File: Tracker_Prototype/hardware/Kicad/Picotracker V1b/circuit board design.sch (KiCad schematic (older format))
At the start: 57 parts, among them IC7 SPV1040, J1 Conn_01x06, J2 GND, J3 +SOL, J4 BATT_V+, J5 BATT_GND, Q1 Q_PMOS_DGS, Q2 Q_PMOS_DGS, SW1 SW_Push, U2 TPS62740, U3 CMWX1ZZABZ-078, U4 MAX-M8C, U6 MS5607-02BA

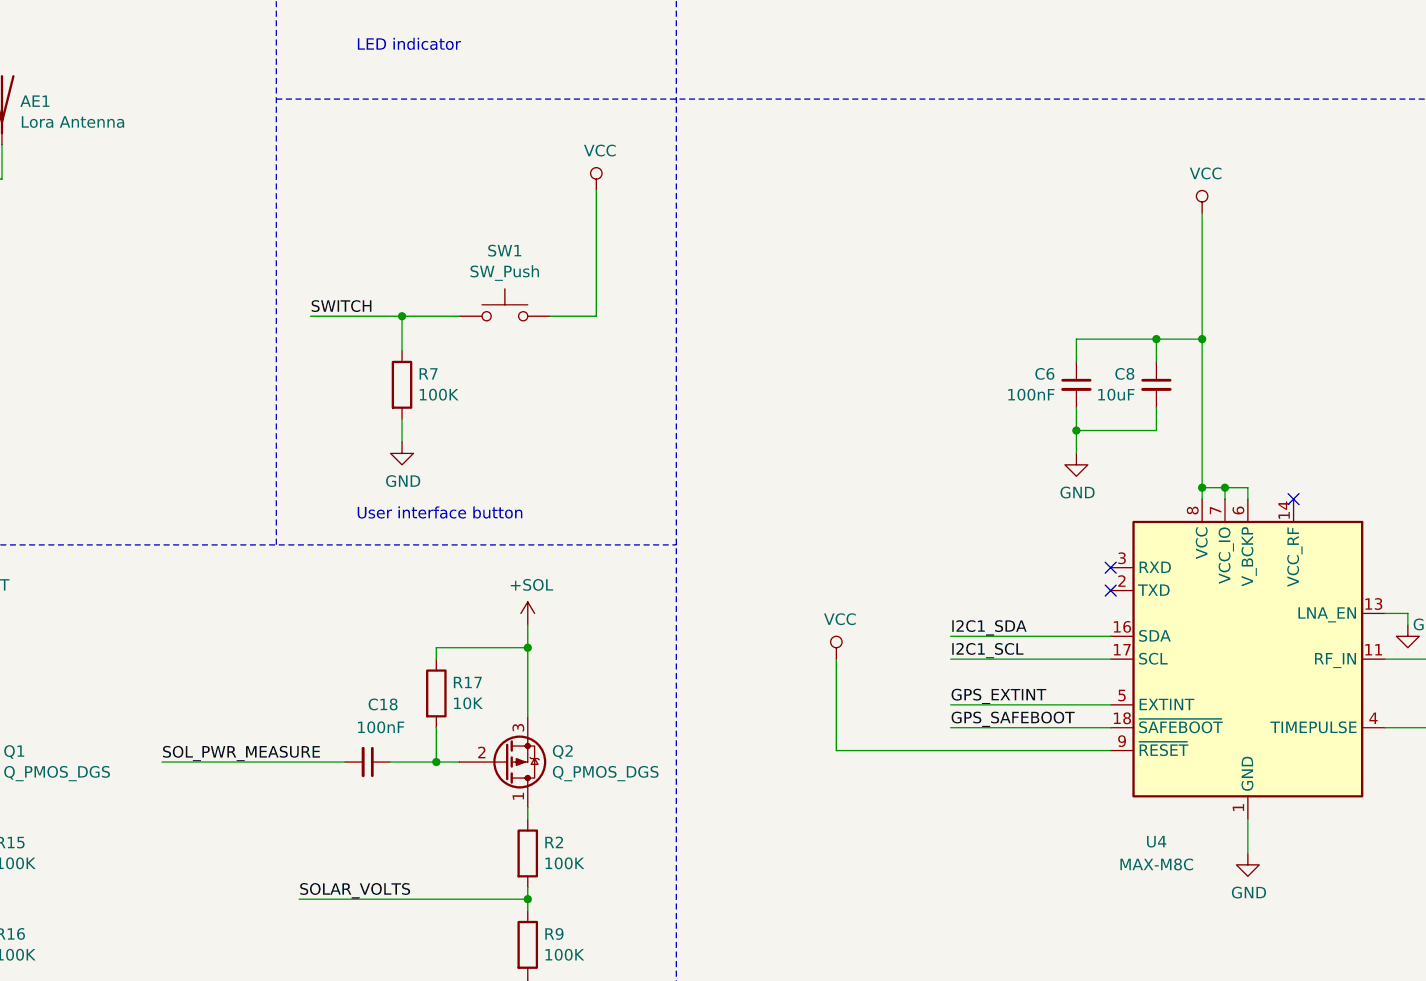
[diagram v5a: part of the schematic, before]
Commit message: Power GPS through SENSE_VCC
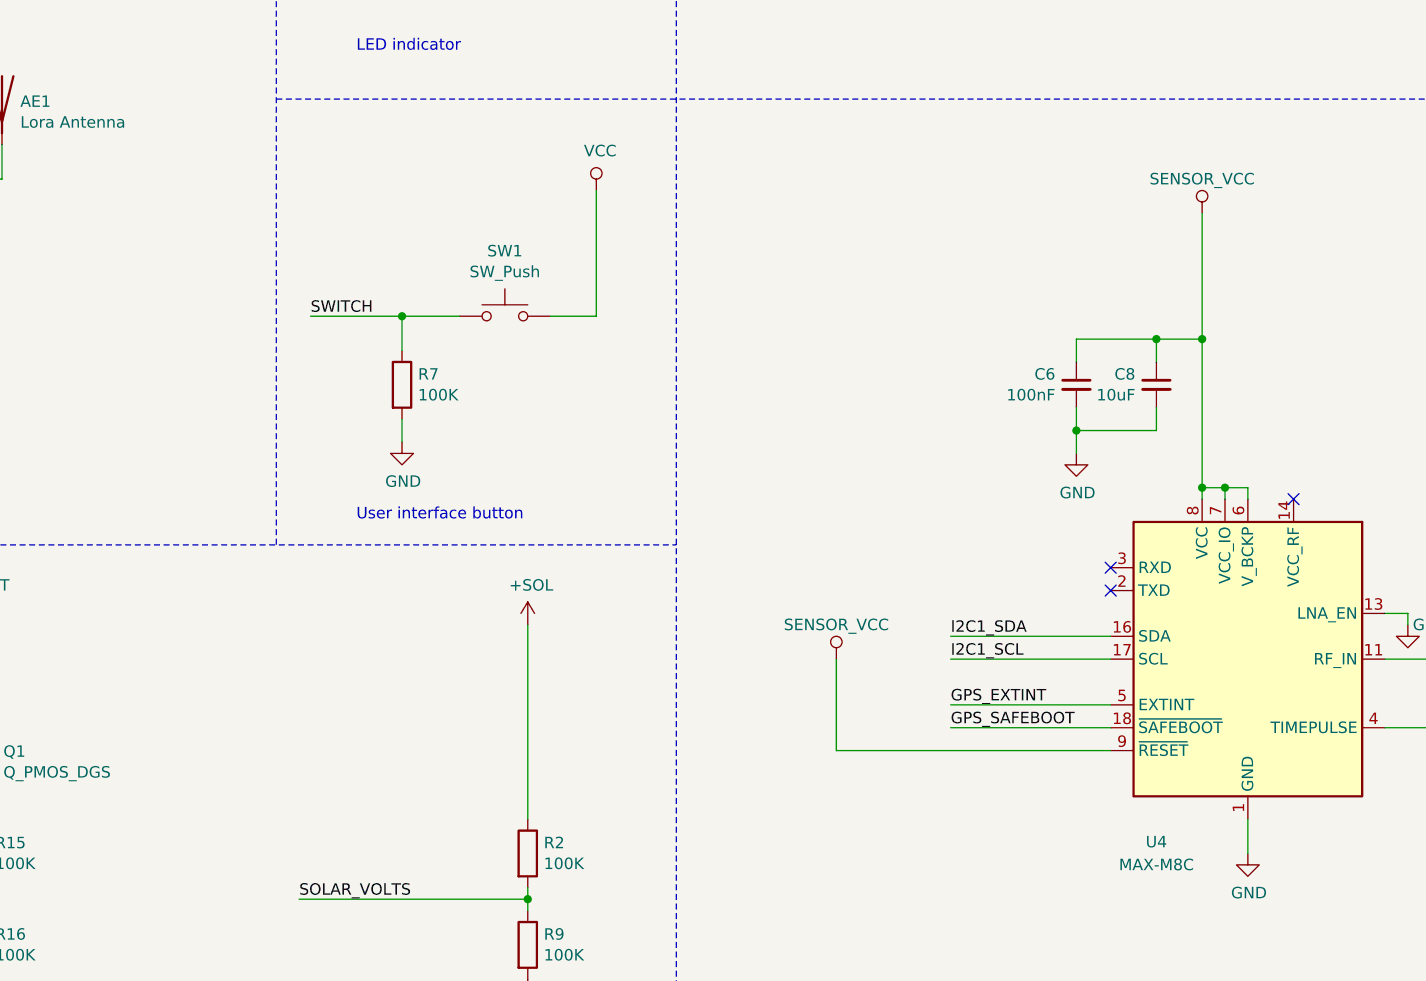
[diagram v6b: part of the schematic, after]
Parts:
- removed C18: 100nF, Capacitor_SMD:C_0402_1005Metric, symbol Device:C_Small
- removed Q2: Q_PMOS_DGS, Package_TO_SOT_SMD:SOT-23, symbol Device:Q_PMOS_DGS
- removed R17: 10K, Resistor_SMD:R_0402_1005Metric, symbol Device:R
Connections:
- net +SOL: now also R2.1
- net SENSOR_VCC: now also C6.1, C8.1, U4.6 (V_BCKP), U4.7 (VCC_IO), U4.8 (VCC), U4.9 (~RESET)
- net VCC: no longer C6.1, C8.1, U4.6 (V_BCKP), U4.7 (VCC_IO), U4.8 (VCC), U4.9 (~RESET)
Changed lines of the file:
@@
-$EndComp
-$Comp
-L power:VCC #PWR024
-U 1 1 5E1179D9
-P 13400 5400
-F 0 "#PWR024" H 13400 5250 50  0001 C CNN
-F 1 "VCC" H 13417 5573 50  0000 C CNN
-F 2 "" H 13400 5400 50  0001 C CNN
-F 3 "" H 13400 5400 50  0001 C CNN
-	1    13400 5400
-	1    0    0    -1
 $EndComp
 $Comp
@@
 Wire Wire Line
 	9250 10300 9600 10300
-$Comp
-L power:VCC #PWR07
-U 1 1 5E22E1C8
-P 11800 7350
-F 0 "#PWR07" H 11800 7200 50  0001 C CNN
-F 1 "VCC" H 11817 7523 50  0000 C CNN
-F 2 "" H 11800 7350 50  0001 C CNN
-F 3 "" H 11800 7350 50  0001 C CNN
-	1    11800 7350
-	1    0    0    -1
-$EndComp
 $Comp
 L Device:L L3
@@
 Text Notes 6300 9100 0    50   ~ 0
 Ultra Low current Solar and Battery voltage measurment
-Wire Wire Line
-	10050 7300 10050 7350
-$Comp
-L Device:C_Small C?
-U 1 1 5DC9D9BB
-P 9750 7800
-AR Path="/5D5B15F7/5DC9D9BB" Ref="C?"  Part="1"
-AR Path="/5DC9D9BB" Ref="C18"  Part="1"
-F 0 "C18" V 9500 7800 50  0000 L CNN
-F 1 "100nF" V 9600 7750 50  0000 L CNN
-F 2 "Capacitor_SMD:C_0402_1005Metric" H 9750 7800 50  0001 C CNN
-F 3 "~" H 9750 7800 50  0001 C CNN
-	1    9750 7800
-	0    1    1    0
-$EndComp
-$Comp
-L Device:R R17
-U 1 1 5DCA03DC
-P 10050 7500
-F 0 "R17" H 10120 7546 50  0000 L CNN
-F 1 "10K" H 10120 7455 50  0000 L CNN
-F 2 "Resistor_SMD:R_0402_1005Metric" V 9980 7500 50  0001 C CNN
-F 3 "~" H 10050 7500 50  0001 C CNN
-	1    10050 7500
-	1    0    0    -1
-$EndComp
-Wire Wire Line
-	10450 7200 10450 7300
-$Comp
-L Device:Q_PMOS_DGS Q2
-U 1 1 5DCBAF0F
-P 10350 7800
-F 0 "Q2" H 10556 7754 50  0000 L CNN
-F 1 "Q_PMOS_DGS" H 10556 7845 50  0000 L CNN
-F 2 "Package_TO_SOT_SMD:SOT-23" H 10550 7900 50  0001 C CNN
-F 3 "~" H 10350 7800 50  0001 C CNN
-	1    10350 7800
-	1    0    0    1
-$EndComp
-Wire Wire Line
-	10450 8000 10450 8050
-Wire Wire Line
-	10050 7300 10450 7300
-Connection ~ 10450 7300
-Wire Wire Line
-	10450 7300 10450 7600
-Wire Wire Line
-	9850 7800 10050 7800
-Wire Wire Line
-	10050 7650 10050 7800
-Connection ~ 10050 7800
-Wire Wire Line
-	10050 7800 10150 7800
-Text Label 8850 7800 0    50   ~ 0
-SOL_PWR_MEASURE
-Wire Wire Line
-	8850 7800 9650 7800
 Wire Wire Line
 	10450 8350 10450 8400
@@
 	1    0    0    -1
 $EndComp
+$Comp
+L flight-computer:SENSOR_VCC #PWR?
+U 1 1 5DBE4A13
+P 11800 7350
+F 0 "#PWR?" H 11800 7200 50  0001 C CNN
+F 1 "SENSOR_VCC" H 11800 7500 50  0000 C CNN
+F 2 "" H 11800 7350 50  0001 C CNN
+F 3 "" H 11800 7350 50  0001 C CNN
+	1    11800 7350
+	1    0    0    -1
+$EndComp
+$Comp
+L flight-computer:SENSOR_VCC #PWR?
+U 1 1 5DBE7B3F
+P 13400 5400
+F 0 "#PWR?" H 13400 5250 50  0001 C CNN
+F 1 "SENSOR_VCC" H 13400 5550 50  0000 C CNN
+F 2 "" H 13400 5400 50  0001 C CNN
+F 3 "" H 13400 5400 50  0001 C CNN
+	1    13400 5400
+	1    0    0    -1
+$EndComp
+Wire Wire Line
+	10450 7200 10450 8050
 $EndSCHEMATC

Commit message: Connected ABZ output pin to GPS back up pin for b variant
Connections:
- net SENSOR_VCC: no longer U4.6 (V_BCKP)
- net GPS_BCKP: now reaches U3.20 (PA8/MCO)
- net GPS_BCKP: now also U4.6 (V_BCKP)
- no-connect marks 30 -> 29
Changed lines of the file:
@@
 NoConn ~ 6700 4950
 NoConn ~ 6700 5050
-NoConn ~ 4900 3550
 NoConn ~ 4900 3450
 NoConn ~ 4900 3050
@@
 Connection ~ 13400 6600
 Wire Wire Line
-	13500 6600 13600 6600
-Connection ~ 13500 6600
-Wire Wire Line
 	11800 7750 11800 7350
 Text Label 12300 7650 0    50   ~ 0
@@
 Wire Wire Line
 	13500 6650 13500 6600
-Wire Wire Line
-	13600 6600 13600 6650
 Wire Wire Line
 	13000 7550 12300 7550
@@
 Wire Wire Line
 	10450 7200 10450 8050
+Wire Wire Line
+	13600 6650 13600 6500
+Wire Wire Line
+	13600 6500 14200 6500
+Text Label 14200 6500 2    50   ~ 0
+GPS_BCKP
+Text Label 4100 3550 0    50   ~ 0
+GPS_BCKP
+Wire Wire Line
+	4100 3550 4900 3550
 $EndSCHEMATC

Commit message: Routed most of the b variant of the board
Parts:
- added J6: ICSS LOGO, flight-computer:ICSS_Logo, symbol Connector_Generic:Conn_01x01
- D2: Purchase link (none) -> https://uk.rs-online.com/web/p/rectifier-diodes-schottky-di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
- L3: footprint Inductor_coilcraft:LPS3015 -> Inductor_SMD:L_Taiyo-Yuden_NR-30xx
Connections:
- net +BATT: now also U2.8 (VSEL4), U2.9 (VSEL3); no longer U2.10 (VSEL2), U2.11 (VSEL1)
- net BATT_PWR_MEASURE: now also U3.20 (PA8/MCO); no longer U3.19 (PA9/USART1_TX)
- net GND: now also U2.10 (VSEL2), U2.11 (VSEL1); no longer U2.8 (VSEL4), U2.9 (VSEL3)
- net GPS_BCKP: now also U3.19 (PA9/USART1_TX); no longer U3.20 (PA8/MCO)
- net SOL_PWR_MEASURE: no longer names the net of U3.18 (PA10/USART1_RX)
- no-connect marks 29 -> 31
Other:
- note added: "ICSS Logo placeholder\n"
- note added: "Output voltage is set to 3V, by setting the VSEL values"
- note removed: "Must adjust values of VSEL pin connections to target output voltage."
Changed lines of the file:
@@
 F 2 "Diode_SMD:D_0402_1005Metric" H 14950 2350 50  0001 C CNN
 F 3 "~" H 14950 2350 50  0001 C CNN
+F 4 "https://uk.rs-online.com/web/p/rectifier-diodes-schottky-diodes/1867707/" H 14950 2350 50  0001 C CNN "Purchase link"
 	1    14950 2350
 	0    1    1    0
@@
 Wire Wire Line
 	2600 8950 2600 9350
-Wire Wire Line
-	3150 9550 3050 9550
-Wire Wire Line
-	3050 9550 3050 9900
 $Comp
 L power:GND #PWR06
 U 1 1 5DF751EA
-P 3050 9900
-F 0 "#PWR06" H 3050 9650 50  0001 C CNN
-F 1 "GND" H 3055 9727 50  0000 C CNN
-F 2 "" H 3050 9900 50  0001 C CNN
-F 3 "" H 3050 9900 50  0001 C CNN
-	1    3050 9900
-	1    0    0    -1
-$EndComp
-Connection ~ 3050 9550
-Wire Wire Line
-	3150 9350 3050 9350
-Wire Wire Line
-	3050 9350 3050 9450
-Wire Wire Line
-	3150 9450 3050 9450
-Connection ~ 3050 9450
-Wire Wire Line
-	3050 9450 3050 9550
-Wire Wire Line
-	3150 9150 3050 9150
-Wire Wire Line
-	3050 9150 3050 9050
+P 2900 9900
+F 0 "#PWR06" H 2900 9650 50  0001 C CNN
+F 1 "GND" H 2905 9727 50  0000 C CNN
+F 2 "" H 2900 9900 50  0001 C CNN
+F 3 "" H 2900 9900 50  0001 C CNN
+	1    2900 9900
+	1    0    0    -1
+$EndComp
 Connection ~ 3050 8950
 Wire Wire Line
 	3050 8950 2600 8950
 Wire Wire Line
-	3150 9250 3050 9250
-Wire Wire Line
-	3050 9250 3050 9150
-Connection ~ 3050 9150
-Wire Wire Line
 	3150 9050 3050 9050
-Connection ~ 3050 9050
 Wire Wire Line
 	3050 9050 3050 8950
@@
 	4550 9550 4550 9950
 $Comp
-L flight-computer:SENSOR_VCC #PWR018
-U 1 1 5E02FB2C
-P 4050 9850
-F 0 "#PWR018" H 4050 9700 50  0001 C CNN
-F 1 "SENSOR_VCC" H 4050 10000 50  0000 C CNN
-F 2 "" H 4050 9850 50  0001 C CNN
-F 3 "" H 4050 9850 50  0001 C CNN
-	1    4050 9850
-	1    0    0    -1
-$EndComp
-$Comp
 L flight-computer:SENSOR_VCC #PWR01
 U 1 1 5E03CB4D
@@
 Text Notes 2100 10550 0    50   ~ 0
 Buck coverter to bring battery voltage down to voltage for GPS and ABZ module
-Text Notes 2850 8100 0    50   ~ 0
-Must adjust values of VSEL pin connections to target output voltage.
 Connection ~ 4550 8950
 $Comp
@@
 F 0 "L3" V 12269 1850 50  0000 C CNN
 F 1 "10uH" V 12360 1850 50  0000 C CNN
-F 2 "Inductor_coilcraft:LPS3015" H 12450 1850 50  0001 C CNN
+F 2 "Inductor_SMD:L_Taiyo-Yuden_NR-30xx" H 12450 1850 50  0001 C CNN
 F 3 "https://www.mouser.co.uk/datasheet/2/597/lps3015-270734.pdf" H 12450 1850 50  0001 C CNN
 	1    12450 1850
@@
 Text Label 4100 3250 0    50   ~ 0
 BATT_VOLTS
-Text Label 4100 3650 0    50   ~ 0
+Text Label 4100 3550 0    50   ~ 0
 BATT_PWR_MEASURE
 Wire Wire Line
-	4900 3650 4100 3650
-Text Label 4100 3750 0    50   ~ 0
-SOL_PWR_MEASURE
-Wire Wire Line
-	4900 3750 4100 3750
+	4900 3550 4100 3550
 Wire Notes Line
 	500  5200 2500 5200
@@
 $EndComp
 $Comp
-L flight-computer:SENSOR_VCC #PWR?
+L flight-computer:SENSOR_VCC #PWR0109
+U 1 1 5DBE7B3F
+P 13400 5400
+F 0 "#PWR0109" H 13400 5250 50  0001 C CNN
+F 1 "SENSOR_VCC" H 13400 5550 50  0000 C CNN
+F 2 "" H 13400 5400 50  0001 C CNN
+F 3 "" H 13400 5400 50  0001 C CNN
+	1    13400 5400
+	1    0    0    -1
+$EndComp
+Wire Wire Line
+	10450 7200 10450 8050
+Wire Wire Line
+	13600 6650 13600 6500
+Wire Wire Line
+	13600 6500 14200 6500
+Text Label 14200 6500 2    50   ~ 0
+GPS_BCKP
+Text Label 4100 3650 0    50   ~ 0
+GPS_BCKP
+Wire Wire Line
+	4100 3650 4900 3650
+NoConn ~ 4900 3750
+$Comp
+L Connector_Generic:Conn_01x01 J6
+U 1 1 5DC88318
+P 13550 9450
+F 0 "J6" H 13630 9492 50  0000 L CNN
+F 1 "ICSS LOGO" H 13630 9401 50  0000 L CNN
+F 2 "flight-computer:ICSS_Logo" H 13550 9450 50  0001 C CNN
+F 3 "~" H 13550 9450 50  0001 C CNN
+	1    13550 9450
+	-1   0    0    1
+$EndComp
+NoConn ~ 13750 9450
+Text Notes 13050 9750 0    50   ~ 0
+ICSS Logo placeholder\n
+Wire Wire Line
+	3150 9450 3050 9450
+Wire Wire Line
+	3050 9450 3050 9350
+Connection ~ 3050 9050
+Wire Wire Line
+	3150 9350 3050 9350
+Connection ~ 3050 9350
+Wire Wire Line
+	3050 9350 3050 9050
+Wire Wire Line
+	3150 9250 2900 9250
+Wire Wire Line
+	2900 9250 2900 9900
+Wire Wire Line
+	3150 9150 2900 9150
+Wire Wire Line
+	2900 9150 2900 9250
+Connection ~ 2900 9250
+Wire Wire Line
+	3150 9550 3150 9900
+$Comp
+L power:GND #PWR0116
+U 1 1 5DD2A631
+P 3150 9900
+F 0 "#PWR0116" H 3150 9650 50  0001 C CNN
+F 1 "GND" H 3155 9727 50  0000 C CNN
+F 2 "" H 3150 9900 50  0001 C CNN
+F 3 "" H 3150 9900 50  0001 C CNN
+	1    3150 9900
+	1    0    0    -1
+$EndComp
+Text Notes 2550 8300 0    50   ~ 0
+Output voltage is set to 3V, by setting the VSEL values
+Wire Wire Line
+	4050 9850 4050 9800
+$Comp
+L flight-computer:SENSOR_VCC #PWR0110
 U 1 1 5DBE4A13
 P 11800 7350
-F 0 "#PWR?" H 11800 7200 50  0001 C CNN
+F 0 "#PWR0110" H 11800 7200 50  0001 C CNN
 F 1 "SENSOR_VCC" H 11800 7500 50  0000 C CNN
 F 2 "" H 11800 7350 50  0001 C CNN
@@
 $EndComp
 $Comp
-L flight-computer:SENSOR_VCC #PWR?
-U 1 1 5DBE7B3F
-P 13400 5400
-F 0 "#PWR?" H 13400 5250 50  0001 C CNN
-F 1 "SENSOR_VCC" H 13400 5550 50  0000 C CNN
-F 2 "" H 13400 5400 50  0001 C CNN
-F 3 "" H 13400 5400 50  0001 C CNN
-	1    13400 5400
-	1    0    0    -1
-$EndComp
-Wire Wire Line
-	10450 7200 10450 8050
-Wire Wire Line
-	13600 6650 13600 6500
-Wire Wire Line
-	13600 6500 14200 6500
-Text Label 14200 6500 2    50   ~ 0
-GPS_BCKP
-Text Label 4100 3550 0    50   ~ 0
-GPS_BCKP
-Wire Wire Line
-	4100 3550 4900 3550
+L flight-computer:SENSOR_VCC #PWR0117
+U 1 1 5DDF39D8
+P 4050 9800
+F 0 "#PWR0117" H 4050 9650 50  0001 C CNN
+F 1 "SENSOR_VCC" H 4067 9973 50  0000 C CNN
+F 2 "" H 4050 9800 50  0001 C CNN
+F 3 "" H 4050 9800 50  0001 C CNN
+	1    4050 9800
+	1    0    0    -1
+$EndComp
 $EndSCHEMATC
